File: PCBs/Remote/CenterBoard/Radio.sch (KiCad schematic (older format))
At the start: 38 parts, among them J801 SMA, U801 nRF24L01P, U802 RFX2401C, X801 16MHz

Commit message: Bezig met LEDS
Signed-off-by: Eldalote.Electronics <Eldalote.Electronics@gmail.com>
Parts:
- removed C807: 1.5pF, Capacitor_SMD:C_0402_1005Metric, symbol Device:C_Small
- removed C809: 1.0pF, Capacitor_SMD:C_0402_1005Metric, symbol Device:C_Small
- removed C814, C815, C816, C817: 1pF, Capacitor_SMD:C_0402_1005Metric, symbol Device:C_Small
- removed C?: 0p3F, Capacitor_SMD:C_0603_1608Metric, symbol Device:C_Small
- removed C? (x4): 1p5F, Capacitor_SMD:C_0402_1005Metric, symbol Device:C_Small
- removed L804, L805: 2.7nH, Inductor_SMD:L_0402_1005Metric, symbol Device:L_Small
- removed L? (x2): 2n4H, Inductor_SMD:L_0603_1608Metric_Pad1.05x0.95mm_HandSolder, symbol Device:L_Small
- removed R804: 2K, Resistor_SMD:R_0402_1005Metric, symbol Device:R_Small
- removed U801: nRF24L01P, Package_DFN_QFN:QFN-20-1EP_4x4mm_P0.5mm_EP2.5x2.5mm, symbol RF:nRF24L01P
- removed U802: RFX2401C, QFN50P300X300X60-17N-D, symbol SamacSys_Parts:RFX2401C
- added C407: 1.5pF, Capacitor_SMD:C_0603_1608Metric_Pad1.05x0.95mm_HandSolder, symbol Device:C_Small
- added C408: 1.0pF, Capacitor_SMD:C_0603_1608Metric_Pad1.05x0.95mm_HandSolder, symbol Device:C_Small
- added U401: nRF24L01P, Eldalote-footprints:nRF24L01P-QFN-20-1EP_4x4mm_P0.5mm_EP, symbol Eldalote-General:nRF24L01P
- added U402: RFX2401C, Package_DFN_QFN:QFN-16-1EP_3x3mm_P0.5mm_EP1.75x1.75mm, symbol Eldalote-General:RFX2401C
- C401: renamed from C801; footprint Capacitor_SMD:C_0402_1005Metric -> Capacitor_SMD:C_0603_1608Metric; LCSC C1585 -> C21117
- C402: renamed from C802; LCSC C1523 -> C1523
- C410: renamed from C810; LCSC C1530 -> C1530
- C411: renamed from C811; LCSC C15195 -> C15195
- C412: renamed from C812; LCSC C52923 -> C52923
- C413: renamed from C813; value 0p3F -> 0.3pF; footprint Capacitor_SMD:C_0805_2012Metric_Pad1.15x1.40mm_HandSolder -> Capacitor_SMD:C_0603_1608Metric_Pad1.05x0.95mm_HandSolder; DigiKey 712-1712-1-ND -> 712-1300-1-ND; Mouser 609-251R15S0R3AV4E -> 609-251R14S0R3AV4T
- L401: renamed from L801; LCSC C16208 -> C16208
- L402: renamed from L802; LCSC C27123 -> C27123
- L403: renamed from L803; LCSC C14033 -> C14033
- R401: renamed from R801; LCSC C25768 -> C25768
- R402: renamed from R802; symbol Device:R_Small -> Device:R; LCSC C11702 -> C11702
- R403: renamed from R803; symbol Device:R_Small -> Device:R
- gave numbers to parts that had none: 1
- renumbered C803 to C403, C804 to C404, C805 to C405, C806 to C406, C808 to C409, J801 to J401, X801 to X401
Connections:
- net labels added: RXEN, TXEN
- wire segments 132 -> 110
- no-connect marks 1 -> 0
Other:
- note added: "Impedance matching notes:\nJLC stackup JLC2313, impedance matching to 50 Ohms;\nTraces of 5.78mil (0.1468mm) wide.\n"
- moved on the sheet: C410, C411, C412, C413, FL401, J401, L403, R402, R403

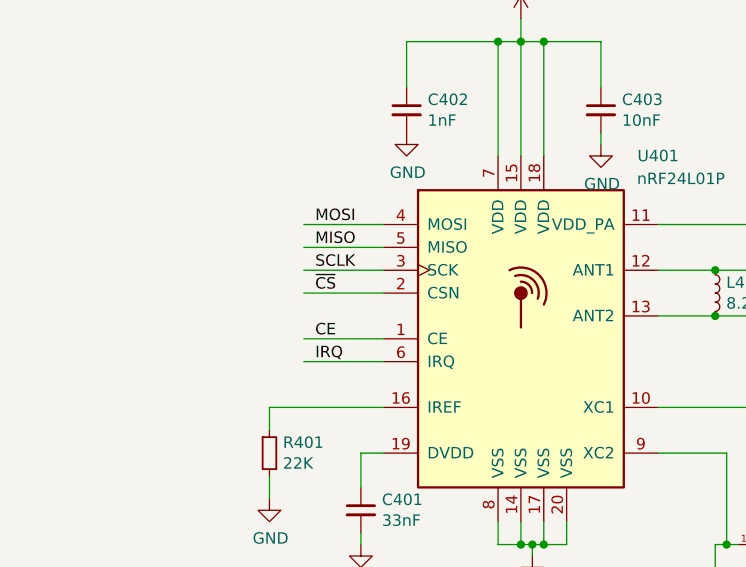
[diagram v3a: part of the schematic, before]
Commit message: Redid the radio PCB layout on both drone and remote PCB. Drone PCB had old schematic, remote PCB layout wasn't ideal.
Copied in the VHDL project files from the seperate VHDL project into the main "All in one" project.

Signed-off-by: Eldalote.Electronics <Eldalote.Electronics@gmail.com>
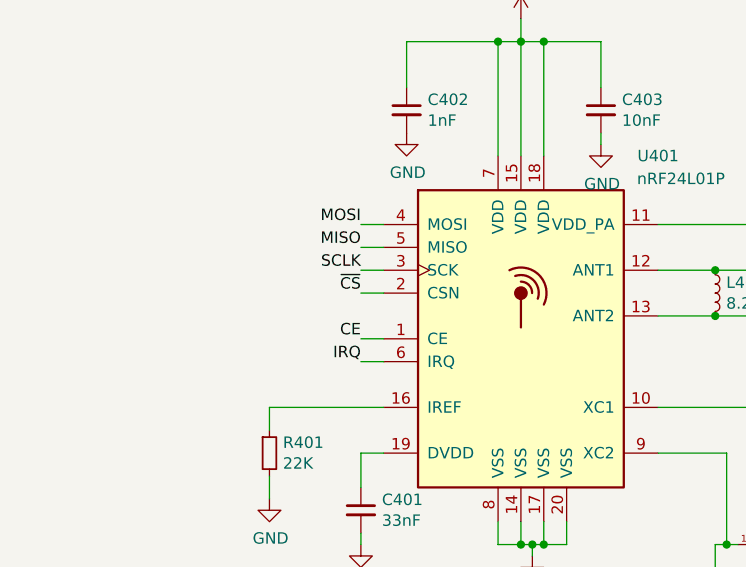
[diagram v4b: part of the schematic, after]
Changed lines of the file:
@@
 $Descr A4 11693 8268
 encoding utf-8
-Sheet 4 7
+Sheet 4 8
 Title ""
 Date ""
@@
 F 2 "Capacitor_SMD:C_0603_1608Metric_Pad1.05x0.95mm_HandSolder" H 7588 3850 50  0001 C CNN
 F 3 "~" H 7550 4000 50  0001 C CNN
-F 4 "" H 7550 4000 50  0001 C CNN "LCSC"
-F 5 "712-1300-1-ND" H 7550 4000 50  0001 C CNN "DigiKey"
-F 6 "609-251R14S0R3AV4T" H 7550 4000 50  0001 C CNN "Mouser"
+F 4 "712-1300-1-ND" H 7550 4000 50  0001 C CNN "DigiKey"
+F 5 "609-251R14S0R3AV4T" H 7550 4000 50  0001 C CNN "Mouser"
 	1    7550 4000
 	-1   0    0    1
@@
 VDD_PA
 Wire Wire Line
-	2200 3400 1850 3400
-Wire Wire Line
-	2200 3500 1850 3500
-Wire Wire Line
-	2200 3600 1850 3600
-Wire Wire Line
-	2200 3700 1850 3700
-Wire Wire Line
-	2200 3900 1850 3900
-Wire Wire Line
-	2200 4000 1850 4000
-Text Label 1900 3400 0    50   ~ 0
+	2200 3400 2100 3400
+Wire Wire Line
+	2200 3500 2100 3500
+Wire Wire Line
+	2200 3600 2100 3600
+Wire Wire Line
+	2200 3700 2100 3700
+Wire Wire Line
+	2200 3900 2100 3900
+Wire Wire Line
+	2200 4000 2100 4000
+Text Label 2100 3400 2    50   ~ 0
 MOSI
-Text Label 1900 3500 0    50   ~ 0
+Text Label 2100 3500 2    50   ~ 0
 MISO
-Text Label 1900 3600 0    50   ~ 0
+Text Label 2100 3600 2    50   ~ 0
 SCLK
-Text Label 1900 3700 0    50   ~ 0
+Text Label 2100 3700 2    50   ~ 0
 ~CS
-Text Label 1900 3900 0    50   ~ 0
+Text Label 2100 3900 2    50   ~ 0
 CE
-Text Label 1900 4000 0    50   ~ 0
+Text Label 2100 4000 2    50   ~ 0
 IRQ
 Wire Wire Line
